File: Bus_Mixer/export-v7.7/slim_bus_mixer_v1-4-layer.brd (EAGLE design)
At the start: 84.8 x 52.5 mm, 149 parts, among them IC1 PCA9539PW, IC10 DG412-JT, IC11 DG412-JT, IC2 TL074JT, IC3 TL072JT, IC4 TL074JT, IC6 TL072JT, IC7 TL074JT, IC8 DG412-JT, IC9 DG412-JT

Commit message: moving to single line for switches + control
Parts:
- IC10, IC11, IC8, IC9: value DG412-JT -> DG412-JS; device joakim:TSSOP16J -> joakim:SO-16
- moved IC8 21.5 mm to (25.1, 27.1)
- moved R87 16.8 mm to (16.4, 27.0)
- moved R89 16.8 mm to (16.4, 25.8)
- moved R91 16.8 mm to (16.4, 29.5)
- moved R93 16.8 mm to (16.4, 28.3)
- moved R97 16.8 mm to (16.4, 30.8)
- moved R86 16.8 mm to (14.3, 27.6)
- moved R88 16.8 mm to (14.3, 26.4)
- moved R90 16.8 mm to (14.3, 30.2)
- moved R92 16.8 mm to (14.3, 28.9)
- moved R96 16.8 mm to (14.3, 31.4)
- moved R72 16.4 mm to (3.49, 24.5)
- moved R83 16.4 mm to (1.43, 25.2)
- moved R94 16.4 mm to (3.49, 26.7)
- moved R95 16.4 mm to (1.43, 27.5)
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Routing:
- net DIG_8_BUS_B: track 67.9 -> 1.73 mm, vias 2 -> 1
- net DIG_8_BUS_A: track 58.1 -> 4.32 mm, vias 2 -> 1
- net DIG_6_BUS_B: track 49.7 -> 1.38 mm, vias 2 -> 0
- net DIG_7_BUS_B: track 47.2 -> 1.70 mm, vias 2 -> 1
- net DIG_7_BUS_A: track 42.5 -> 4.48 mm, vias 1 -> 0
- net DIG_6_BUS_A: track 40.6 -> 4.64 mm, vias 1 -> 0
- net BUS_B: track 99.4 -> 71.4 mm, vias 5 -> 6
- net BUS_A: track 103.7 -> 76.9 mm, vias 6 -> 7
- net DIG_1_BUS_B: track 28.1 -> 1.75 mm, vias 1 -> 0
- net DIG_5_BUS_B: track 26.8 -> 1.70 mm, vias 2 -> 0
- net VL: track 78.1 -> 53.4 mm, vias 0 -> 4
- net DIG_1_BUS_A: track 24.6 -> 3.72 mm, vias 1 -> 0
- net BUS_FX_B: track 46.2 -> 26.6 mm, vias 3 -> 2
- net DIG_3_BUS_A: track 21.7 -> 4.34 mm, vias 1 -> 0
- net DIG_5_BUS_A: track 21.7 -> 4.48 mm, vias 1 -> 0
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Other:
- outline, holes or cut-outs redrawn

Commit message: Probably at max compression, still needs cleanup
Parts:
- moved C25 16.5 mm to (62.5, 28.9), turned to 180 degrees
- moved R80 15.5 mm to (62.5, 27.8), turned to 180 degrees
- moved R79 15.1 mm to (62.5, 19.8), turned to 180 degrees
- moved C24 14.7 mm to (62.5, 18.7), turned to 180 degrees
- moved R97 14.2 mm to (2.70, 27.1), turned to 180 degrees
- moved IC4 13.5 mm to (64.6, 23.8)
- moved C27 13.5 mm to (66.7, 28.9), turned to 0 degrees
- moved R76 13.4 mm to (68.9, 26.2), turned to 270 degrees
- moved R75 13.2 mm to (68.9, 21.0)
- moved R96 12.8 mm to (2.70, 26.1), turned to 180 degrees
- moved R82 12.2 mm to (66.7, 27.8), turned to 0 degrees
- moved R81 11.3 mm to (66.7, 19.8), turned to 0 degrees
- moved C26 10.8 mm to (66.7, 18.7), turned to 0 degrees
- moved R50 10.4 mm to (54.0, 6.19)
- moved C31 10.3 mm to (64.1, 28.3)
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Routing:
- net DIG_7_BUS_A: track 4.48 -> 76.6 mm, vias 0 -> 2
- net DIG_8_BUS_B: track 1.73 -> 70.5 mm, vias 1 -> 2
- net DIG_8_BUS_A: track 4.32 -> 67.9 mm, vias 1 -> 2
- net DIG_6_BUS_A: track 4.64 -> 62.2 mm, vias 0 -> 2
- net DIG_7_BUS_B: track 1.70 -> 59.2 mm, vias 1 -> 2
- net DIG_5_BUS_A: track 4.48 -> 50.4 mm, vias 0 -> 2
- net DIG_6_BUS_B: track 1.38 -> 45.3 mm, vias 0 -> 2
- net DIG_4_BUS_A: track 3.29 -> 46.6 mm, vias 0 -> 2
- net +12V: track 244.7 -> 207.0 mm, vias 13 -> 15
- net DIG_5_BUS_B: track 1.70 -> 34.3 mm, vias 0 -> 2
- net DIG_3_BUS_A: track 4.34 -> 35.9 mm, vias 0 -> 2
- net -12V: track 235.2 -> 207.3 mm
- net OUT2: track 17.2 -> 42.9 mm
- net DIG_2_BUS_A: track 9.86 -> 32.7 mm, vias 0 -> 2
- net DIG_1_BUS_A: track 3.72 -> 21.9 mm, vias 0 -> 2
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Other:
- board size 84.8 x 52.5 mm -> 84.8 x 38.4 mm

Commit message: Last commit without changing the schematics
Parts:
- moved R70 9.38 mm to (67.9, 1.43)
- moved R77 2.83 mm to (31.0, 27.1), turned to 270 degrees
- moved R78 2.42 mm to (32.4, 27.1), turned to 90 degrees
- moved R47 1.85 mm to (82.5, 15.3)
- moved R74 0.40 mm to (60.3, 25.9)
- moved R76 0.32 mm to (68.9, 25.9)
- moved IC1 0.32 mm to (10.2, 23.8)
- moved R86 0.32 mm to (15.5, 24.0)
- moved R87 0.32 mm to (15.5, 22.9)
- moved R88 0.32 mm to (15.5, 21.9)
- moved R89 0.32 mm to (15.5, 20.9)
- moved R90 0.32 mm to (15.5, 26.0)
- moved R91 0.32 mm to (15.5, 25.0)
- moved R92 0.32 mm to (15.5, 27.1)
- moved R93 0.32 mm to (15.5, 28.1)
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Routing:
- net GND: track 72.6 -> 85.5 mm, vias 57 -> 65
- net +3V3: track 39.7 -> 44.4 mm, vias 2 -> 3
- net OUT7: track 20.7 -> 24.1 mm
- net VL: track 59.6 -> 62.8 mm, vias 4 -> 5
- net -12V: track 207.3 -> 209.8 mm, vias 13 -> 15
- net +12V: track 207.0 -> 209.2 mm
- net SUM_FX_A: track 27.1 -> 29.1 mm
- net N$19: track 19.0 -> 17.3 mm
- net DIG_8_BUS_B: track 70.5 -> 68.9 mm
- net OUT1: track 27.8 -> 26.3 mm
- net SDA: track 35.9 -> 37.4 mm
- net SCL: track 38.0 -> 39.5 mm
- net SUM_B: track 57.0 -> 55.9 mm
- net CON5: track 16.5 -> 15.5 mm
- net DIG_8_BUS_A: track 67.9 -> 67.0 mm
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
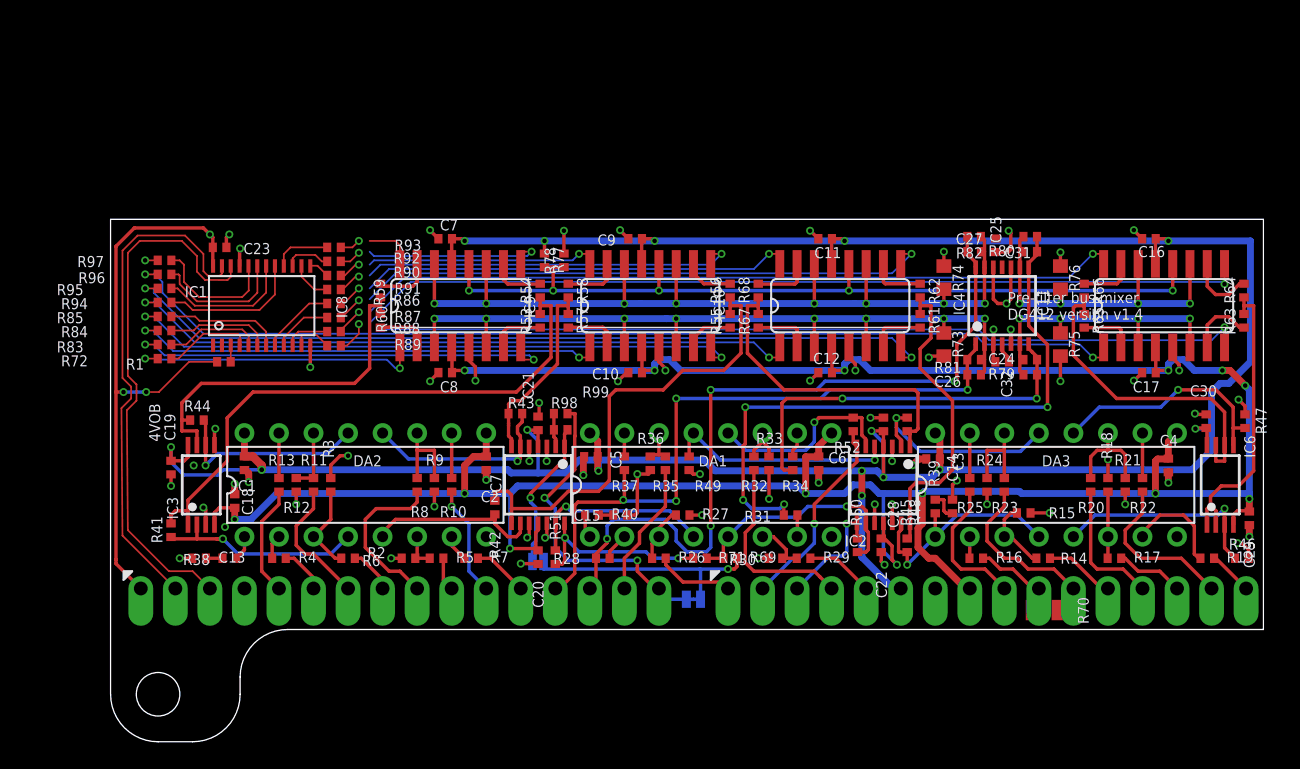
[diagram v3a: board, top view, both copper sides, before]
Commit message: Rotated op amp to better suit power lines
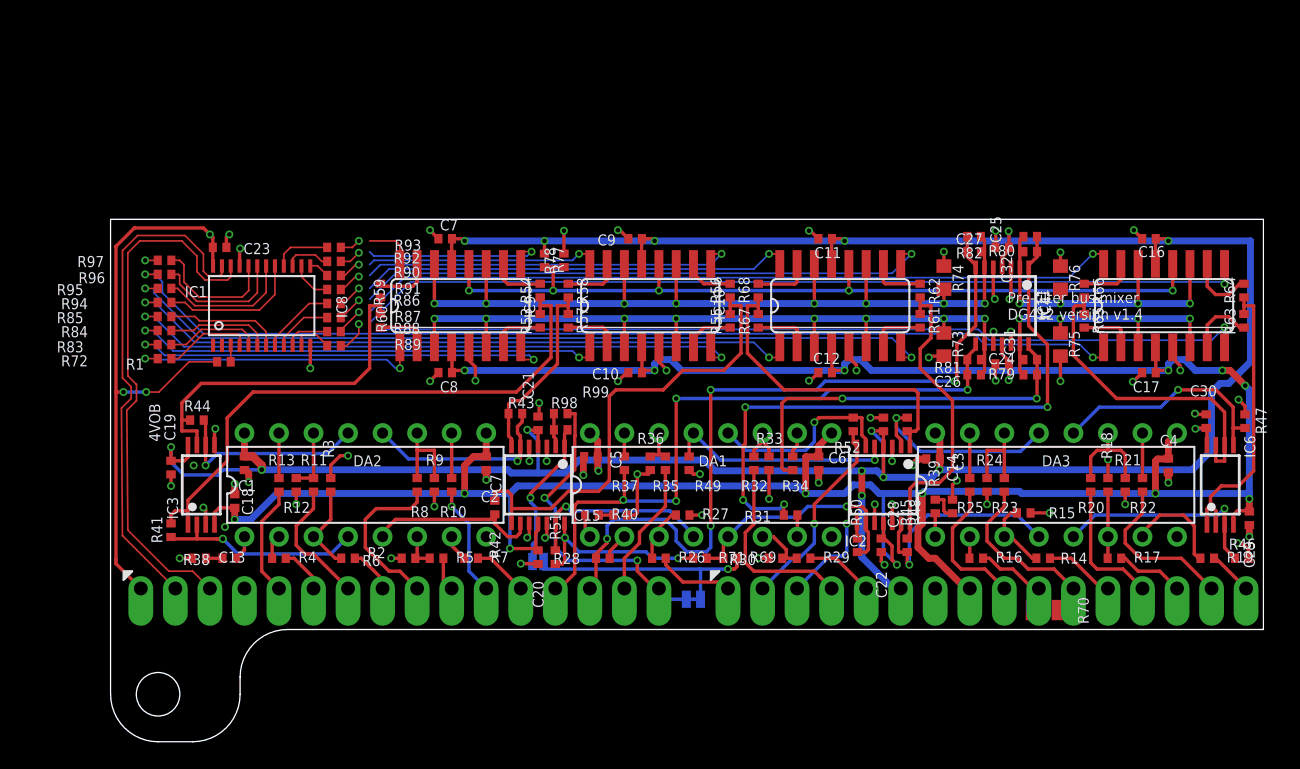
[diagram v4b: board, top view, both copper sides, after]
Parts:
- moved C31 8.74 mm to (64.6, 19.5), turned to 180 degrees
- moved C32 8.41 mm to (64.6, 28.1)
- turned IC4 to 180 degrees
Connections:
- net BUS_A: now also IC4.9; no longer IC4.2
- net BUS_B: now also IC4.6; no longer IC4.13
- net BUS_FX_A: now also IC4.13; no longer IC4.6
- net BUS_FX_B: now also IC4.2; no longer IC4.9
- net SUM_A: now also IC4.8; no longer IC4.1
- net SUM_B: now also IC4.7; no longer IC4.14
- net SUM_FX_A: now also IC4.14; no longer IC4.7
- net SUM_FX_B: now also IC4.1; no longer IC4.8
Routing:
- net +12V: track 209.2 -> 211.2 mm, vias 15 -> 16
- net CON6: track 15.6 -> 16.9 mm
- net -12V: track 209.8 -> 210.8 mm
- net GND: track 85.5 -> 86.1 mm, vias 65 -> 68

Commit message: Everything but fuckup-protection-resistor routed
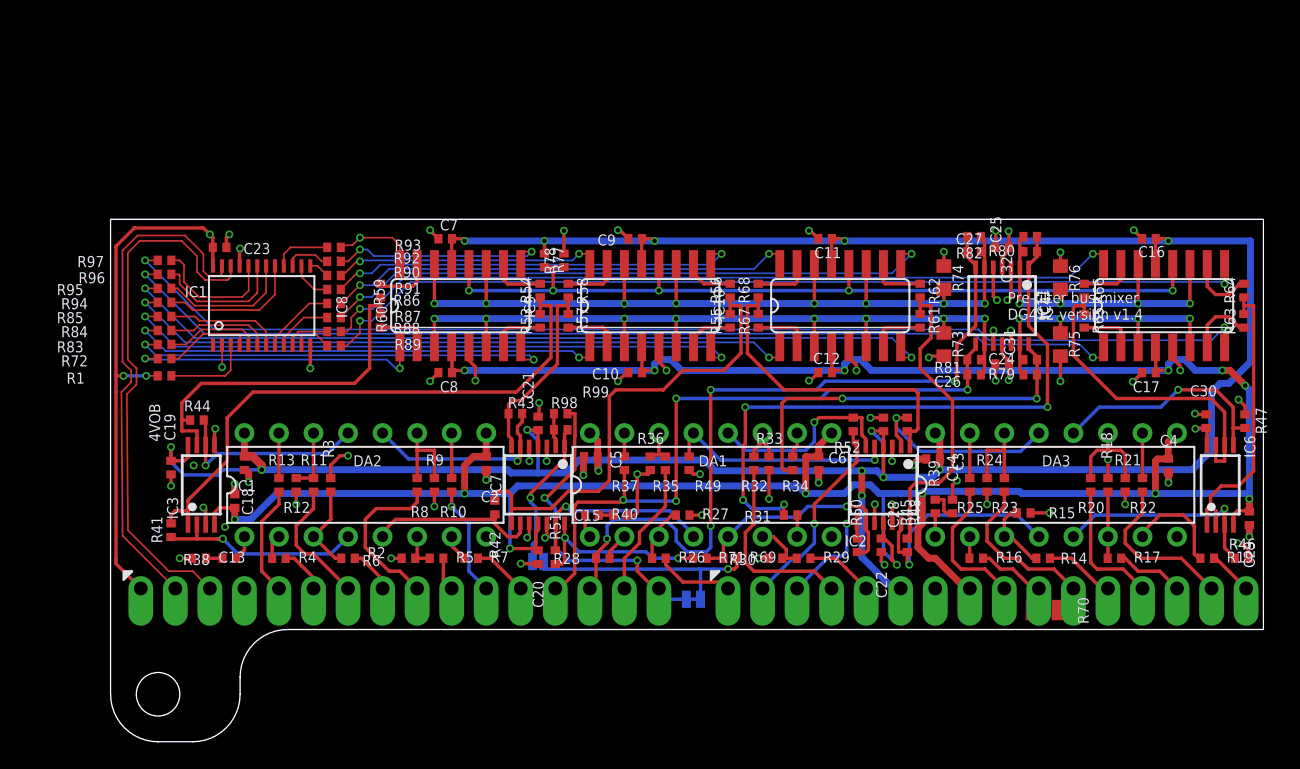
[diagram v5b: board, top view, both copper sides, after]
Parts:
- moved R1 4.49 mm to (3.02, 18.7)
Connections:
- net DIG_1_BUS_B: now also R93.2; no longer R83.2
- net DIG_2_BUS_A: now also R83.2; no longer R84.2
- net DIG_2_BUS_B: now also R92.2; no longer R85.2
- net DIG_3_BUS_A: now also R84.2; no longer R94.2
- net DIG_3_BUS_B: now also R90.2; no longer R95.2
- net DIG_4_BUS_A: now also R85.2; no longer R96.2
- net DIG_4_BUS_B: now also R91.2; no longer R97.2
- net DIG_5_BUS_A: now also R94.2; no longer R92.2
- net DIG_5_BUS_B: now also R86.2; no longer R93.2
- net DIG_6_BUS_A: now also R95.2; no longer R90.2
- net DIG_6_BUS_B: now also R87.2; no longer R91.2
- net DIG_7_BUS_A: now also R96.2; no longer R86.2
- net DIG_7_BUS_B: now also R88.2; no longer R87.2
- net DIG_8_BUS_A: now also R97.2; no longer R88.2
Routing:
- net DIG_8_BUS_A: track 67.0 -> 85.3 mm
- net +3V3: track 44.4 -> 39.1 mm
- net !RST: track 1.21 -> 6.37 mm
- net GND: track 86.1 -> 88.1 mm, vias 68 -> 69
- net DIG_4_BUS_B: track 29.9 -> 31.5 mm
- net DIG_2_BUS_B: track 15.6 -> 17.3 mm
- net DIG_1_BUS_B: track 5.51 -> 7.09 mm
- net DIG_3_BUS_B: track 19.1 -> 20.6 mm
- net DIG_7_BUS_B: track 59.2 -> 60.5 mm
- net DIG_5_BUS_B: track 34.3 -> 35.4 mm
- net DIG_6_BUS_B: track 45.3 -> 46.3 mm
- net DIG_8_BUS_B: track 68.9 -> 69.8 mm
- net DIG_1_BUS_A: track 21.6 -> 22.5 mm
- net DIG_7_BUS_A: track 76.3 -> 75.5 mm
- net DIG_3_BUS_A: track 35.6 -> 36.3 mm
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
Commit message: Finished except perhaps holes and DNM resistor for noise gain
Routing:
- net OUT7: track 24.1 -> 24.6 mm
- net OUT5: track 24.4 -> 24.9 mm
- net GND: vias 69 -> 133
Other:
- board size 84.8 x 38.4 mm -> 84.8 x 30.2 mm
